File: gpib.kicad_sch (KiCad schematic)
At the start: 2 parts, among them U1 SN74LVC8T245PWR, U2 SN74LVC07APWR

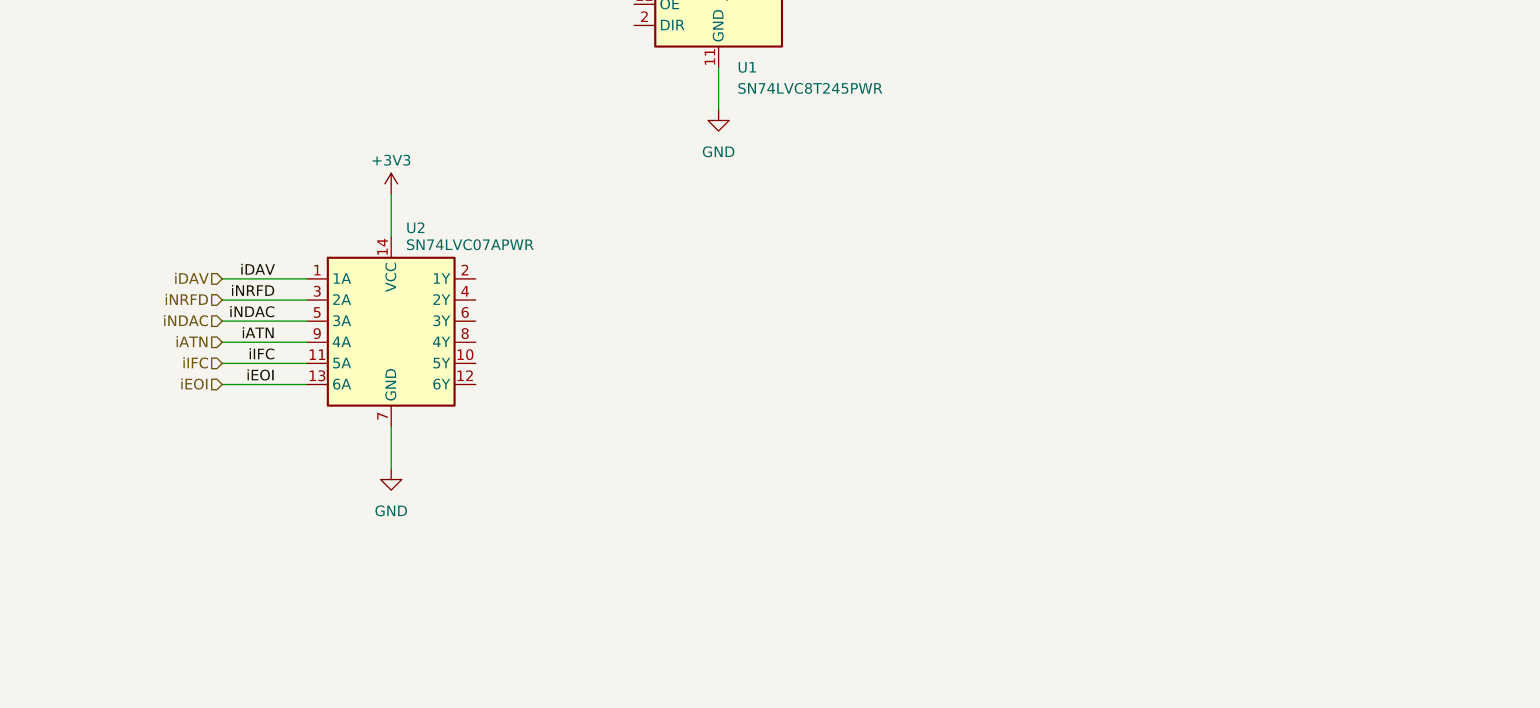
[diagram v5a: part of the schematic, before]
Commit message: Add Schmitt-Trig sense IC, connect GPIB conn nets and run jobfile
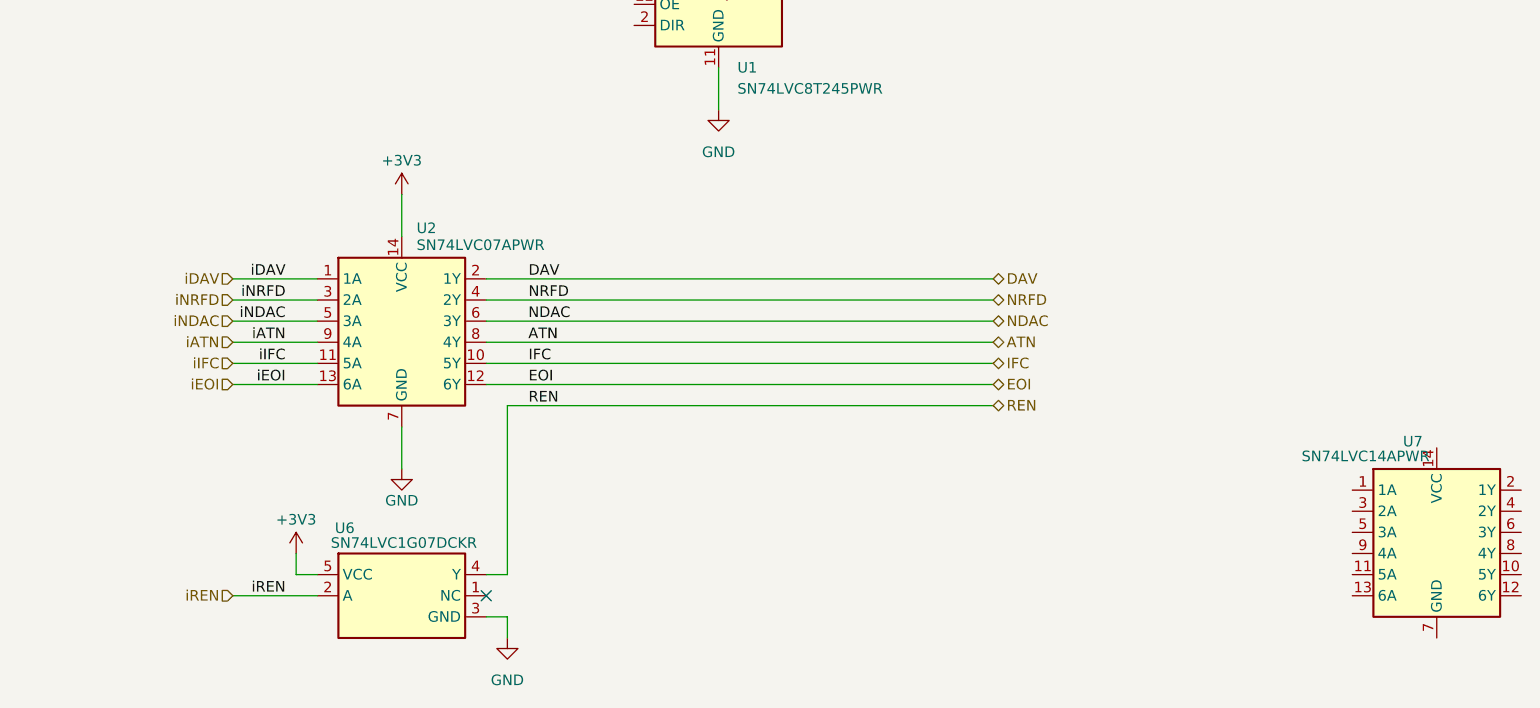
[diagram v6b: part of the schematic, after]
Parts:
- added U6: SN74LVC1G07DCKR, Package_TO_SOT_SMD:SOT-353_SC-70-5, symbol PARTSDB:SN74LVC1G07DCKR
- added U7: SN74LVC14APWR, Package_SO:TSSOP-14_4.4x5mm_P0.65mm, symbol PARTSDB:SN74LVC14APWR
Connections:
- net +3V3: now also U6.5 (VCC)
- net GND: now also U6.3 (GND)
- net IFC: now reaches U2.10 (5Y)
- net EOI: now reaches U2.12 (6Y)
- net DAV: now reaches U2.2 (1Y)
- net NRFD: now reaches U2.4 (2Y)
- net NDAC: now reaches U2.6 (3Y)
- net ATN: now reaches U2.8 (4Y)
- new net REN: U6.4 (Y)
- new net iREN: U6.2 (A)
- no-connect marks 0 -> 1
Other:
- moved on the sheet: U2

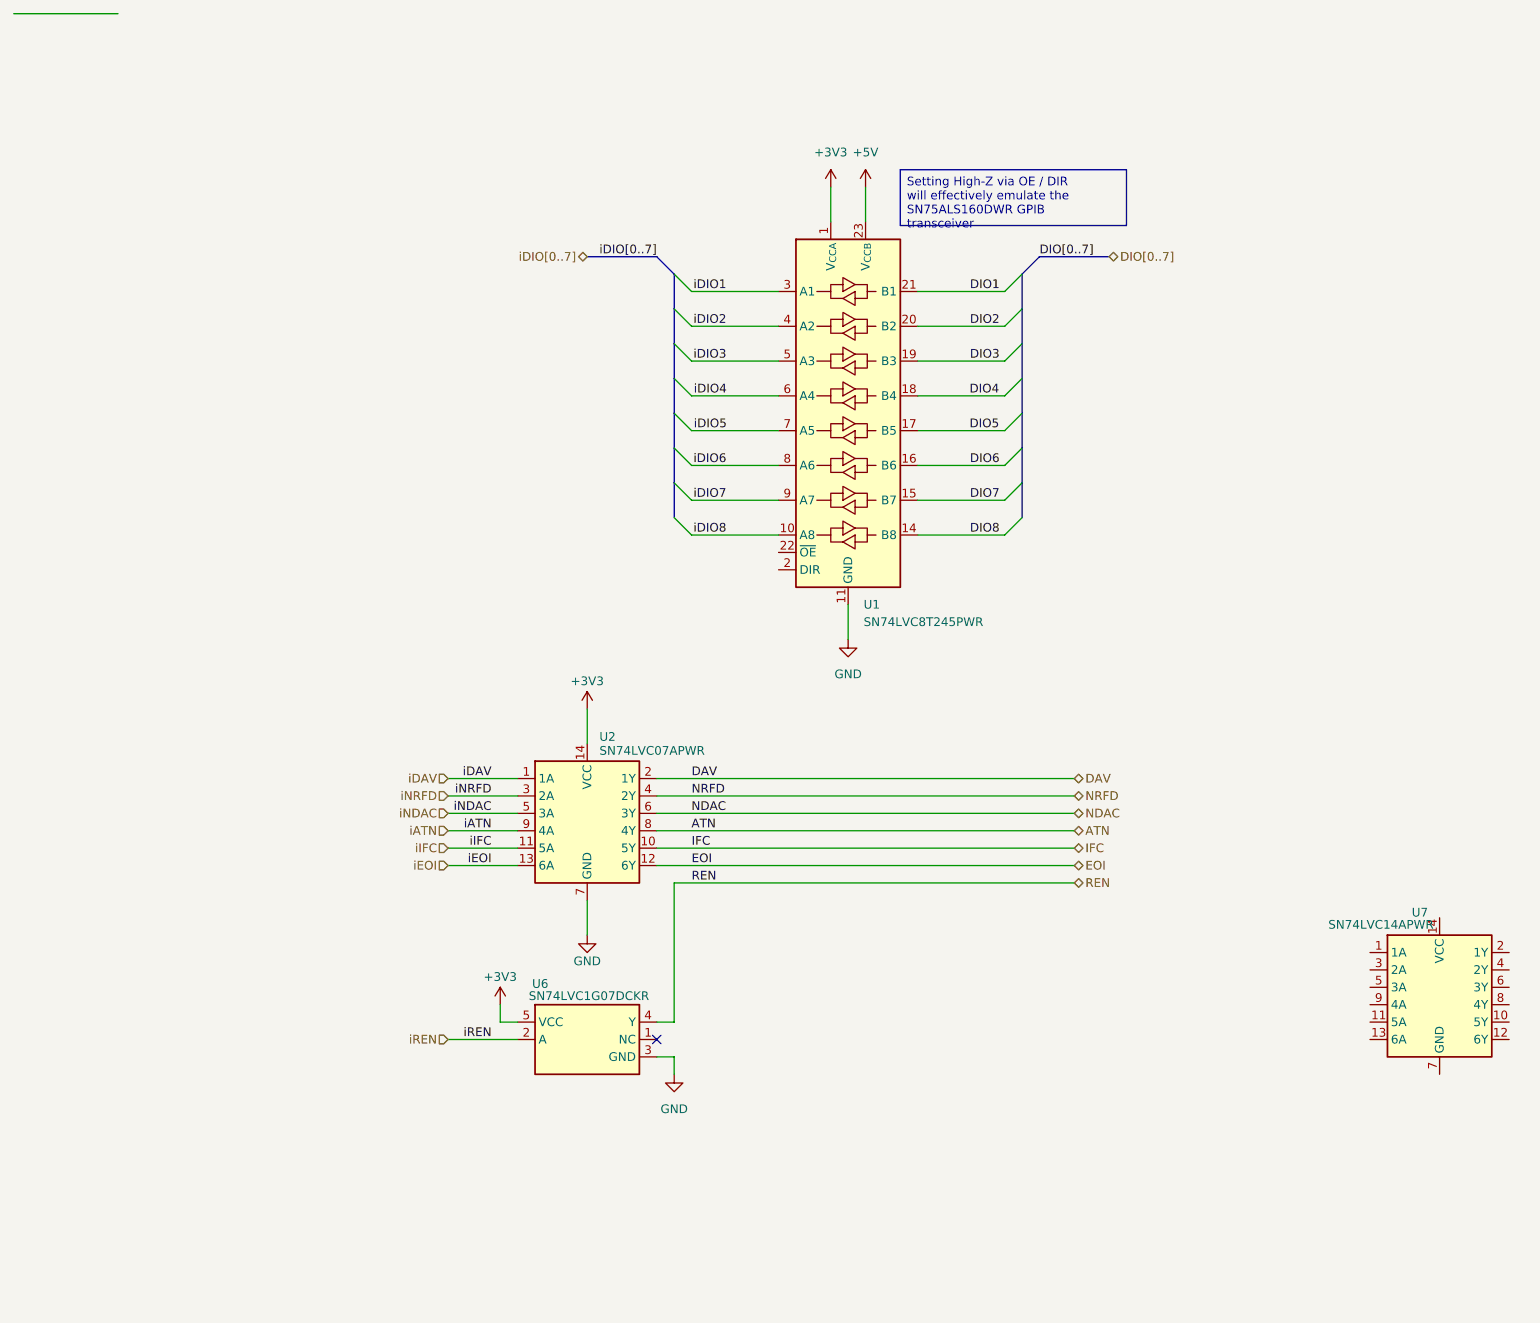
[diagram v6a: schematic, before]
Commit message: Add GPIB interface
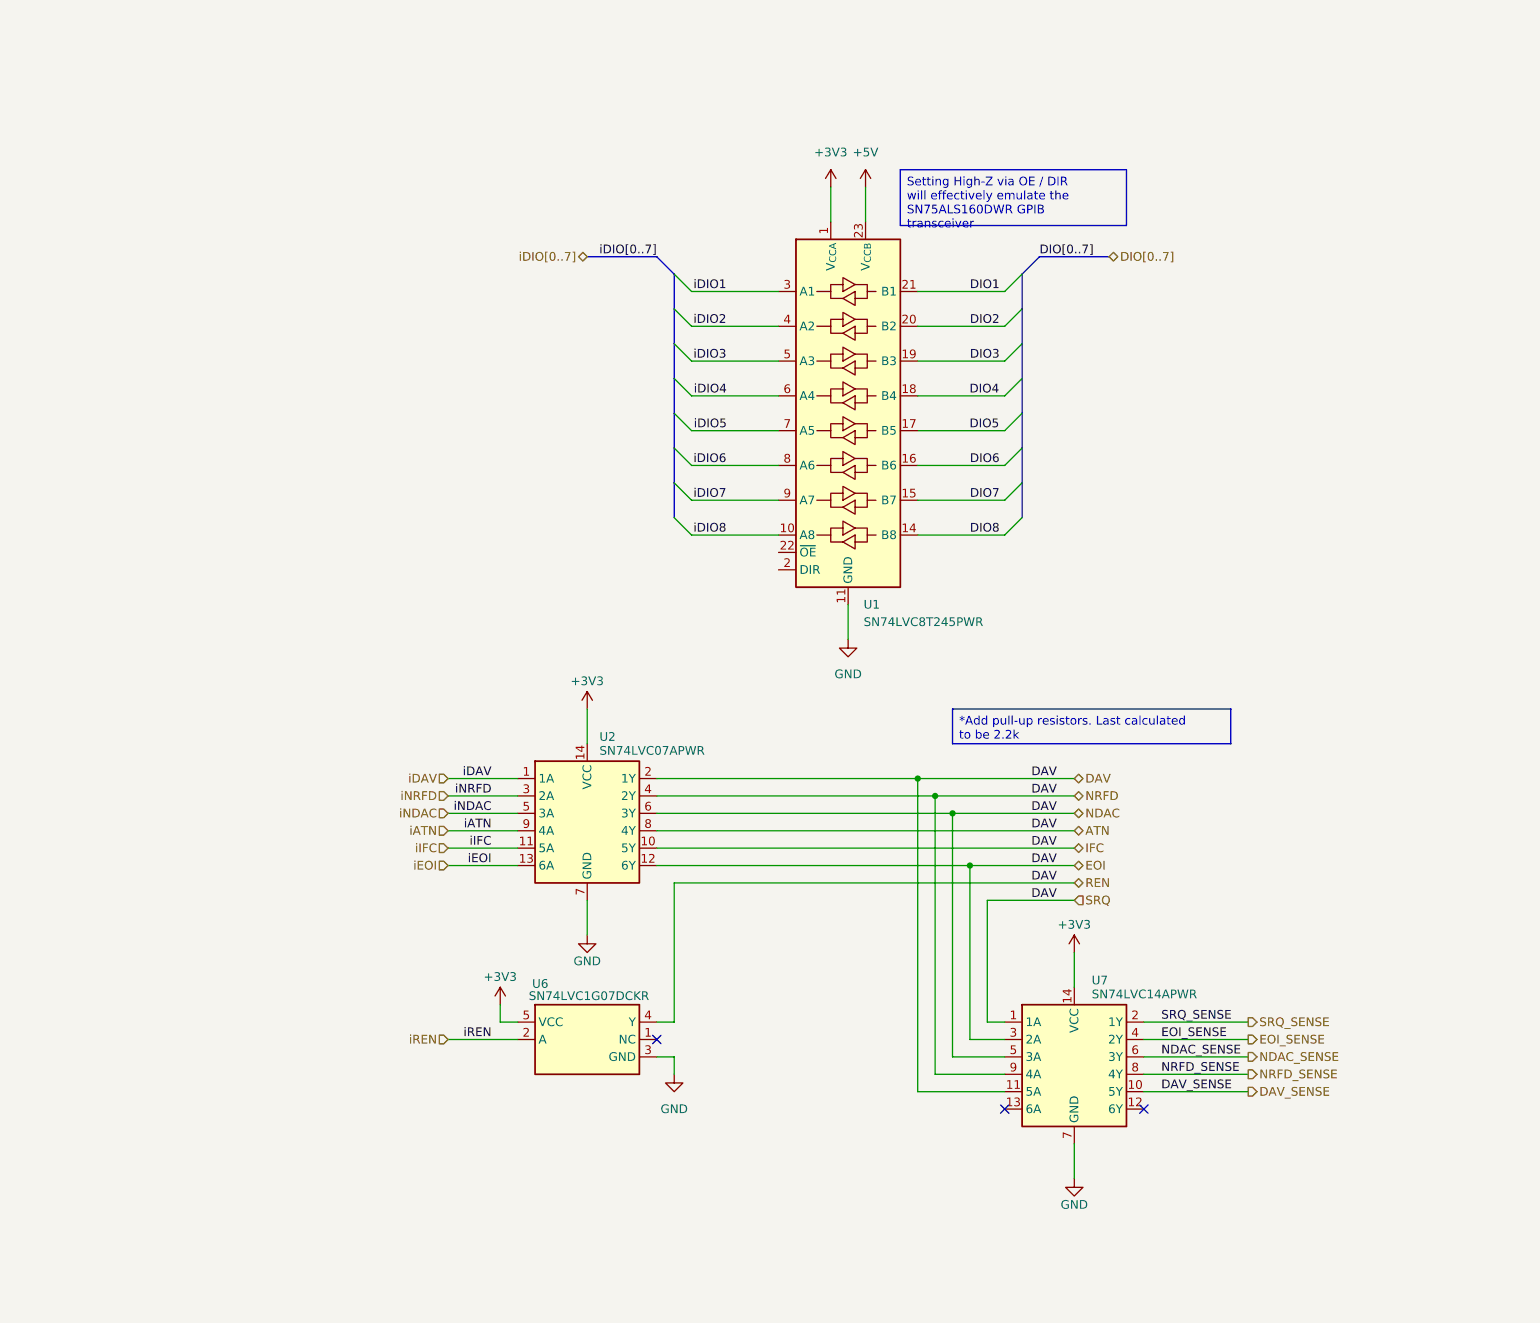
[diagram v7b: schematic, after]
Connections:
- net DAV is gone; now on net ATN: U2.2 (1Y)
- net EOI is gone; now on net ATN: U2.12 (6Y)
- net IFC is gone; now on net ATN: U2.10 (5Y)
- net NDAC is gone; now on net ATN: U2.6 (3Y)
- net NRFD is gone; now on net ATN: U2.4 (2Y)
- net REN is gone; now on net ATN: U6.4 (Y)
- net +3V3: now also U7.14 (VCC)
- net ATN: now also U7.1 (1A), U7.11 (5A), U7.3 (2A), U7.5 (3A), U7.9 (4A)
- net GND: now also U7.7 (GND)
- net DAV_SENSE: now reaches U7.10 (5Y)
- net SRQ_SENSE: now reaches U7.2 (1Y)
- net EOI_SENSE: now reaches U7.4 (2Y)
- net NDAC_SENSE: now reaches U7.6 (3Y)
- net NRFD_SENSE: now reaches U7.8 (4Y)
- no-connect marks 1 -> 3
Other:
- moved on the sheet: U7

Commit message: Finish up schematics
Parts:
- added R8: 2.2k, Resistor_SMD:R_Array_Convex_8x0602, symbol PARTSDB:EXB-2HV222JV
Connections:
- net +5V: now also R8.10 (R7.2), R8.11 (R6.2), R8.12 (R5.2), R8.13 (R4.2), R8.14 (R3.2), R8.15 (R2.2), R8.16 (R1.2), R8.9 (R8.2)
- net ATN: now also R8.1 (R1.1), R8.2 (R2.1), R8.3 (R3.1), R8.4 (R4.1), R8.5 (R5.1), R8.6 (R6.1), R8.7 (R7.1), R8.8 (R8.1)
- net DIO5: now also U1.17 (B5)
- net iDIO5: now also U1.7 (A5)
- net GPIB_DIR: now reaches U1.2 (DIR)
- net GPIB_EN: now reaches U1.22 (~{OE})
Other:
- title: (none) -> GPIB Transceiver
- moved on the sheet: U1, U2, U6, U7
